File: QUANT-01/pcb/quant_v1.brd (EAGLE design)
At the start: 128.6 x 40.3 mm, 0 parts

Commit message: built the base schematic.
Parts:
- added B1: ARDUINO_PRO_MINI, SparkFun-Boards:ARDUINO_PRO_MINI
- added C1: 0.33uF, SparkFun-Capacitors:CAP-PTH-10MM
- added C2: 0.1uF, SparkFun-Capacitors:CAP-PTH-10MM
- added C3, C4: 100uF, SparkFun-Capacitors:CPOL-RADIAL-5MM-10MM
- added D1, D2: 1n5158, adafruit:DO41-10
- added D10, D3, D4, D5, D6, D7, D8, D9: (no value), SparkFun-LED:LED_3MM
- added MCP4725: (no value), SparkFun-Connectors:1X06_NO_SILK
- added MPR121: (no value), SparkFun-Connectors:1X07
- added MPR121_TOUCH_PINS: (no value), SparkFun-Connectors:1X13
- added R1, R2, R3, R4, R5, R6, R7, R8: 330ohm, SparkFun-Resistors:AXIAL-0.3
- added SW1, SW2, SW3, SW4: SUBMINI_SPDT, MusicThingModular:SUBMINI_TOGGLE
- added TL7805: (no value), SparkFun-IC-Power:DC-DC_CONVERTER_78XX
- added U$1: EURO_POWER_LOCK, MusicThingModular:EURO_PWR_HEADER_LOCK
- added U$3, U$4: FB, adafruit:FB
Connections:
- new net +12V: C1.1, TL7805.VIN
- new net -12V: U$1.NEG1, U$1.NEG2, U$4.P$2
- new net 5V: B1.21, B1.24, C2.1, C3.+, C4.-, D1.C, D2.A, MCP4725.3, MPR121.7, SW1.3, SW2.3, SW3.3, SW4.3, TL7805.VOUT
- new net A0: MCP4725.6
- new net GND: B1.23, B1.4, C1.2, C2.2, C3.-, C4.+, D10.K, D3.K, D4.K, D5.K, D6.K, D7.K, D8.K, D9.K, MCP4725.2, MPR121.5, MPR121_TOUCH_PINS.1, SW1.1, SW2.1, SW3.1, SW4.1, TL7805.GND, U$1.GND1, U$1.GND2, U$1.GND3, U$1.GND4, U$1.GND5, U$1.GND6
- new net N$1: U$1.POS1, U$1.POS2, U$3.P$2
- new net N$10: B1.10, R6.P$2
- new net N$11: B1.11, R7.P$2
- new net N$12: B1.12, R8.P$2
- new net N$13: D10.A, R8.P$1
- new net N$14: D9.A, R7.P$1
- new net N$15: D8.A, R6.P$1
- new net N$16: D7.A, R5.P$1
- new net N$17: D6.A, R4.P$1
- new net N$18: D5.A, R3.P$1
- new net N$19: D4.A, R2.P$1
- new net N$2: D2.C, U$4.P$1
- new net N$3: D1.A, U$3.P$1
- new net N$4: B1.5, R1.P$2
- new net N$5: D3.A, R1.P$1
- new net N$6: B1.6, R2.P$2
- new net N$7: B1.7, R3.P$2
- new net N$8: B1.8, R4.P$2
- new net N$9: B1.9, R5.P$2
- new net SCL: B1.A5, MCP4725.5, MPR121.2
- new net SDA: B1.A4, MCP4725.4, MPR121.3
- new net SW1: B1.13, SW4.COM
- new net SW2: B1.14, SW3.COM
- new net SW3: B1.15, SW2.COM
- new net SW4: B1.16, SW1.COM
- new net TOUCH0: MPR121_TOUCH_PINS.2
- new net TOUCH1: MPR121_TOUCH_PINS.3
- new net TOUCH10: MPR121_TOUCH_PINS.12
- new net TOUCH11: MPR121_TOUCH_PINS.13
- new net TOUCH2: MPR121_TOUCH_PINS.4
- new net TOUCH3: MPR121_TOUCH_PINS.5
- new net TOUCH4: MPR121_TOUCH_PINS.6
- new net TOUCH5: MPR121_TOUCH_PINS.7
- new net TOUCH6: MPR121_TOUCH_PINS.8
- new net TOUCH7: MPR121_TOUCH_PINS.9
- new net TOUCH8: MPR121_TOUCH_PINS.10
- new net TOUCH9: MPR121_TOUCH_PINS.11
- new net VOUT: MCP4725.1

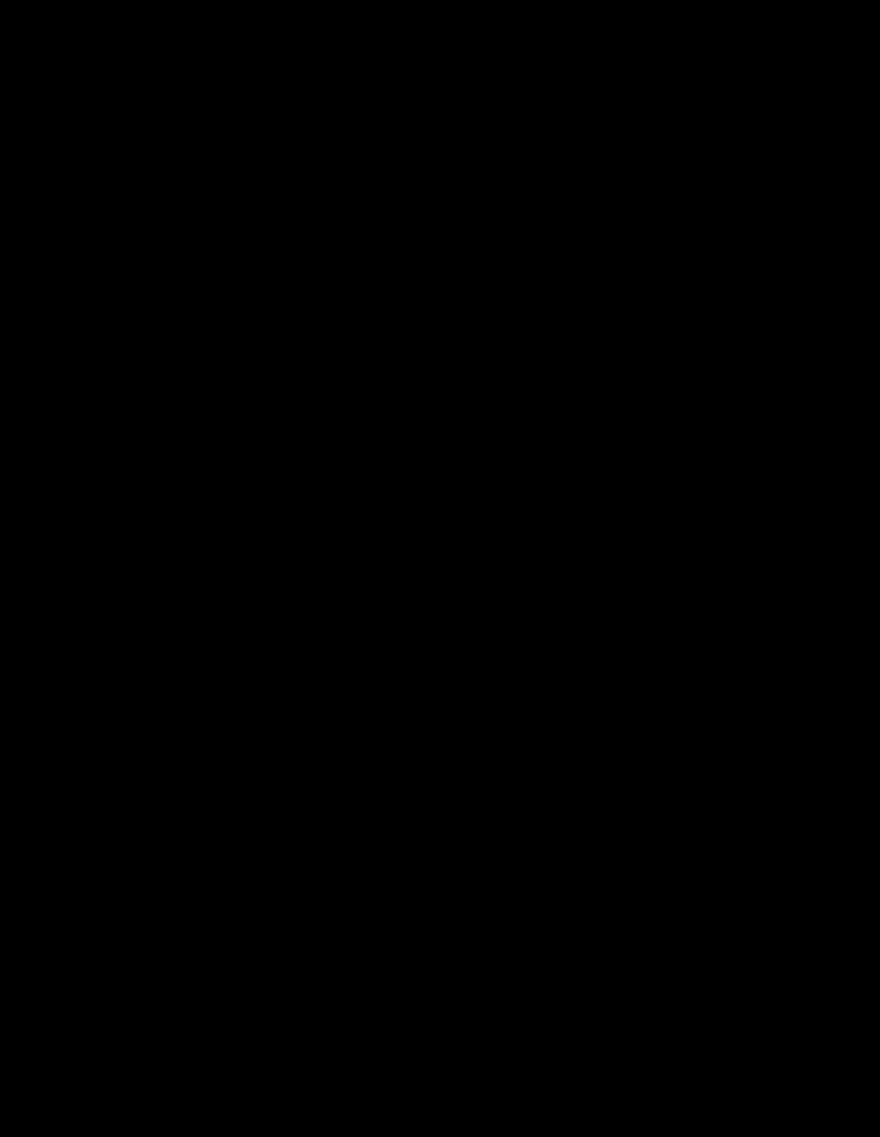
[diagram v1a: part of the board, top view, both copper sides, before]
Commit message: added simple GATE out code.
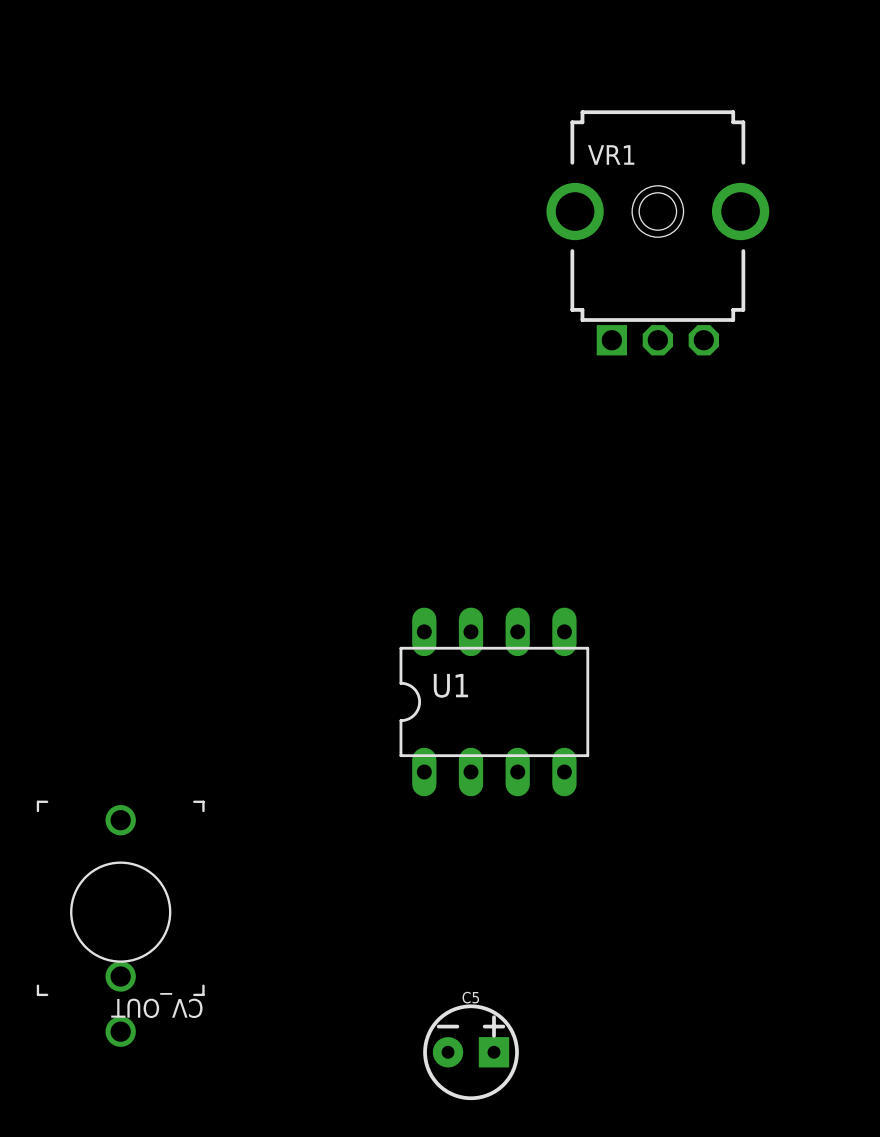
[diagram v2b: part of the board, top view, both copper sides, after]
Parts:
- added C5: 10uF, SparkFun-Capacitors:CPOL-RADIAL-2.5MM-5MM
- added CV_OUT: THONKICONNNEW, MusicThingModular:WQP-PJ301M-12_JACK
- added U1: TL072_, MusicThingModular:DIL08
- added VR1: (no value), MusicThingModular:9MM_SNAP-IN_POT
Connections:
- removed net VOUT: MCP4725.1
- new net N$20: MCP4725.1, U1.3
- new net N$21: U1.1, U1.2, VR1.2, VR1.3
- new net N$23: C5.1, U1.5, VR1.1
- new net N$25: CV_OUT.P$1_TIP, U1.6, U1.7
- new net V+: U1.8
- new net V-: U1.4
- net GND: now also C5.2, CV_OUT.P$3_SLEEVE
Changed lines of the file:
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@@
 <attribute name="PROD_ID" value="RES-08380" x="13.97" y="-604.52" size="1.778" layer="27" display="off"/>
 </element>
+<element name="VR1" library="MusicThingModular" package="9MM_SNAP-IN_POT" value="" x="20.32" y="-629.92"/>
+<element name="U1" library="MusicThingModular" package="DIL08" value="TL072_" x="11.43" y="-656.59"/>
+<element name="C5" library="SparkFun-Capacitors" package="CPOL-RADIAL-2.5MM-5MM" value="10uF" x="10.16" y="-675.64">
+<attribute name="PROD_ID" value="CAP-08440" x="10.16" y="-675.64" size="1.778" layer="27" display="off"/>
+</element>
+<element name="CV_OUT" library="MusicThingModular" package="WQP-PJ301M-12_JACK" value="THONKICONNNEW" x="-8.89" y="-668.02"/>
 </elements>
 <signals>
@@
 <contactref element="D5" pad="K"/>
 <contactref element="D4" pad="K"/>
+<contactref element="C5" pad="2"/>
+<contactref element="CV_OUT" pad="P$3_SLEEVE"/>
 <wire x1="12.7" y1="-452.12" x2="12.7" y2="-471.17" width="0" layer="19" extent="1-1"/>
 <wire x1="12.7" y1="-433.07" x2="12.7" y2="-452.12" width="0" layer="19" extent="1-1"/>
@@
 <wire x1="83.82" y1="27.94" x2="69.85" y2="12.62" width="0" layer="19" extent="1-1"/>
 <wire x1="105.41" y1="15.24" x2="86.36" y2="3.81" width="0" layer="19" extent="1-1"/>
+<wire x1="-8.89" y1="-674.52" x2="12.7" y2="-471.17" width="0" layer="19" extent="1-1"/>
+<wire x1="8.91" y1="-675.64" x2="-8.89" y2="-674.52" width="0" layer="19" extent="1-1"/>
 </signal>
 <signal name="SDA">
@@
 <contactref element="MCP4725" pad="6"/>
 </signal>
-<signal name="VOUT">
-<contactref element="MCP4725" pad="1"/>
-</signal>
 <signal name="TOUCH0">
 <contactref element="MPR121_TOUCH_PINS" pad="2"/>
@@
 <wire x1="10.16" y1="-356.87" x2="10.16" y2="-490.22" width="0" layer="19" extent="1-1"/>
 </signal>
+<signal name="V+">
+<contactref element="U1" pad="8"/>
+</signal>
+<signal name="V-">
+<contactref element="U1" pad="4"/>
+</signal>
+<signal name="N$20">
+<contactref element="MCP4725" pad="1"/>
+<contactref element="U1" pad="3"/>
+<wire x1="81.28" y1="27.94" x2="12.7" y2="-660.4" width="0" layer="19" extent="1-1"/>
+</signal>
+<signal name="N$21">
+<contactref element="U1" pad="1"/>
+<contactref element="VR1" pad="3"/>
+<contactref element="VR1" pad="2"/>
+<contactref element="U1" pad="2"/>
+<wire x1="10.16" y1="-660.4" x2="7.62" y2="-660.4" width="0" layer="19" extent="1-1"/>
+<wire x1="20.32" y1="-636.92" x2="10.16" y2="-660.4" width="0" layer="19" extent="1-1"/>
+<wire x1="22.82" y1="-636.92" x2="20.32" y2="-636.92" width="0" layer="19" extent="1-1"/>
+</signal>
+<signal name="N$23">
+<contactref element="VR1" pad="1"/>
+<contactref element="U1" pad="5"/>
+<contactref element="C5" pad="1"/>
+<wire x1="15.24" y1="-652.78" x2="11.41" y2="-675.64" width="0" layer="19" extent="1-1"/>
+<wire x1="17.82" y1="-636.92" x2="15.24" y2="-652.78" width="0" layer="19" extent="1-1"/>
+</signal>
+<signal name="N$25">
+<contactref element="U1" pad="7"/>
+<contactref element="CV_OUT" pad="P$1_TIP"/>
+<contactref element="U1" pad="6"/>
+<wire x1="10.16" y1="-652.78" x2="-8.89" y2="-663.02" width="0" layer="19" extent="1-1"/>
+<wire x1="12.7" y1="-652.78" x2="10.16" y2="-652.78" width="0" layer="19" extent="1-1"/>
+</signal>
 </signals>

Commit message: started building board.
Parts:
- removed U1: TL072_, MusicThingModular:DIL08
- added C7: 47pf, SparkFun-Capacitors:CAP-PTH-10MM
- added C8, C9: 100nf, SparkFun-Capacitors:CAP-PTH-10MM
- added CV_INPUT: THONKICONNNEW, MusicThingModular:WQP-PJ301M-12_JACK
- added D11: (no value), SparkFun-LED:LED_3MM
- added GATE_OUT: GATE_OUT, MusicThingModular:WQP-PJ301M-12_JACK
- added R10, R11, R17, R18, R9: 100k, SparkFun-Resistors:AXIAL-0.3
- added R12: 49.9k, SparkFun-Resistors:AXIAL-0.3
- added R13, R19, R20: 10k, SparkFun-Resistors:AXIAL-0.3
- added R14, R21: 1k, SparkFun-Resistors:AXIAL-0.3
- added SW5_MODE: SUBMINI_SPDT, MusicThingModular:SUBMINI_TOGGLE
- added U3: MCP6002, MusicThingModular:DIL08
- added U4: TL074_, MusicThingModular:DIL14
- moved C5 738.4 mm to (-16.5, 62.2)
- moved R8 682.0 mm to (-58.4, 73.7)
- moved CV_OUT 676.8 mm to (-48.3, 7.62)
- moved R7 662.1 mm to (-48.3, 73.7)
- moved VR1 645.1 mm to (-69.8, 8.89)
- moved R6 642.2 mm to (-38.1, 73.7)
- moved R5 622.4 mm to (-27.9, 73.7)
- moved R4 602.8 mm to (-17.8, 73.7)
- moved R3 583.7 mm to (-68.6, 68.6)
- moved R2 563.5 mm to (-58.4, 68.6)
- moved D10 541.8 mm to (-35.6, 68.6)
- moved D9 522.4 mm to (-30.5, 68.6)
- moved D8 503.0 mm to (-25.4, 68.6)
- moved D7 483.6 mm to (-20.3, 68.6)
- moved D6 464.3 mm to (-15.2, 68.6)
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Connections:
- removed net V+: U1.8
- removed net V-: U1.4
- new net N$22: CV_INPUT.P$1_TIP, R9.P$1
- new net N$24: R10.P$2, R9.P$2, U4.2
- new net N$26: B1.18, R13.P$2
- new net N$27: R13.P$1, SW5_MODE.COM
- new net N$28: R10.P$1, R11.P$2, U4.1
- new net N$29: R11.P$1, R12.P$2, U3.2
- new net N$30: R17.P$1, R18.P$1, U3.5
- new net N$31: GATE_OUT.P$1_TIP, R21.P$1
- new net N$32: R14.P$2, U4.13
- new net N$33: D11.A, R14.P$1, U4.14
- new net N$37: B1.19, R20.P$2, U4.12
- new net N$38: C7.2, R19.P$2, R20.P$1, U3.6
- new net N$39: C7.1, R19.P$1, R21.P$2, U3.7
- new net VEE: B1.17, R12.P$1, U3.1
- net 5V: now also C8.1, C9.1, R17.P$2, U3.8, U4.11, U4.4
- net GND: now also C8.2, C9.2, CV_INPUT.P$3_SLEEVE, D11.K, GATE_OUT.P$3_SLEEVE, R18.P$2, SW5_MODE.1, U3.3, U3.4, U4.3
- net N$20: now also U4.5; no longer U1.3
- net N$21: now also U4.6, U4.7; no longer U1.1, U1.2
- net N$23: now also U4.10; no longer U1.5
- net N$25: now also U4.8, U4.9; no longer U1.6, U1.7
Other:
- board size 128.6 x 40.3 mm -> 127 x 81.3 mm
- board text removed: "10HP"
- board text removed: "EURORACK PCB BREADBOARD V1.0"

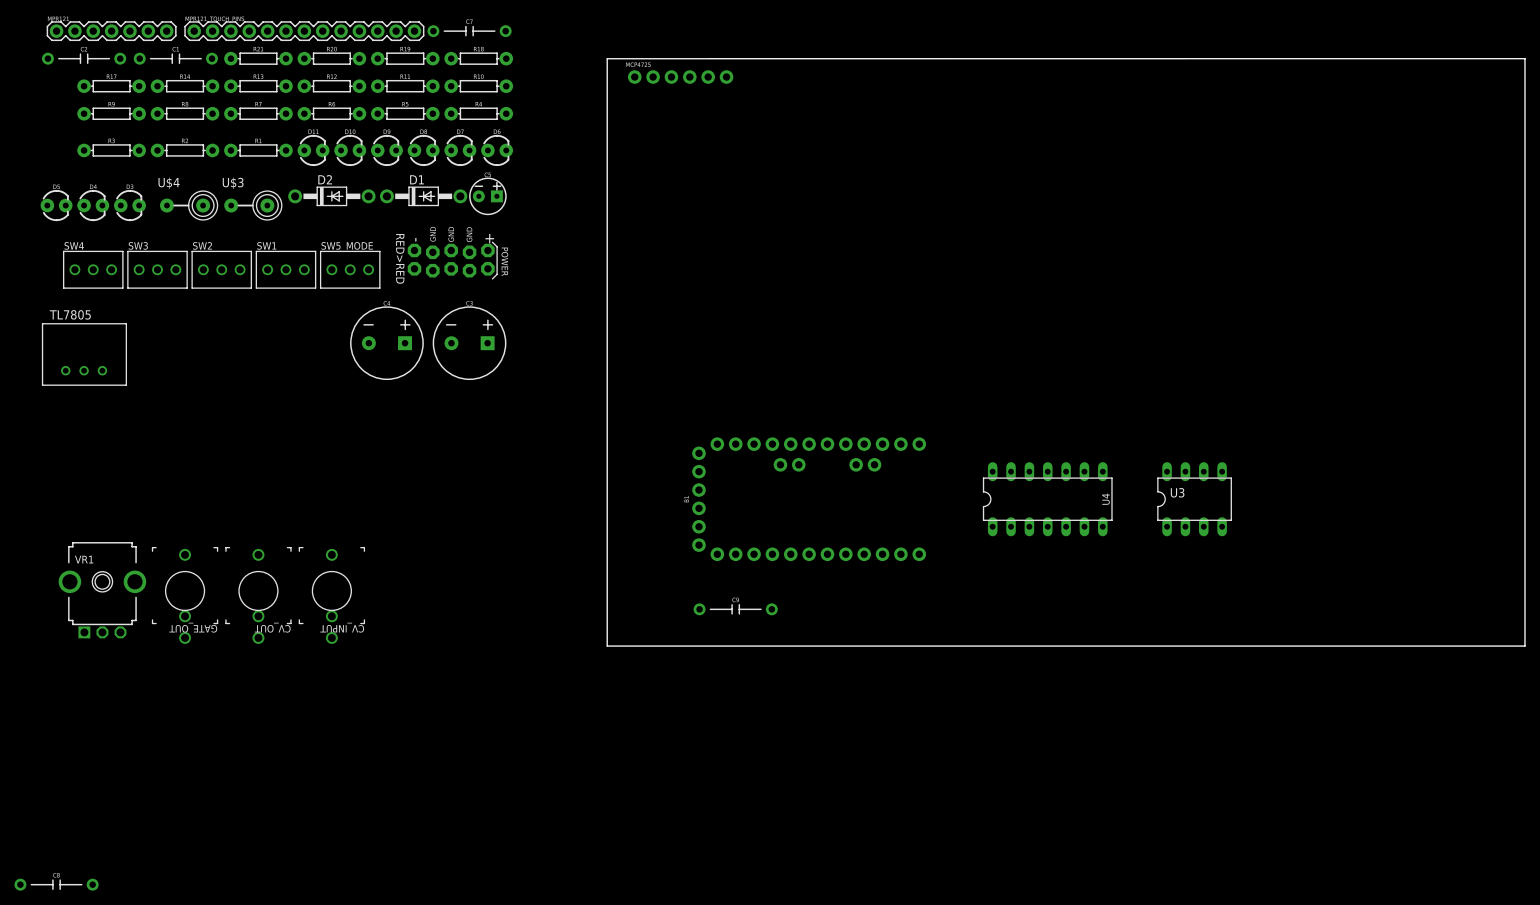
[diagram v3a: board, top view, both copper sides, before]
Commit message: got bottom pcb basic layout in place.
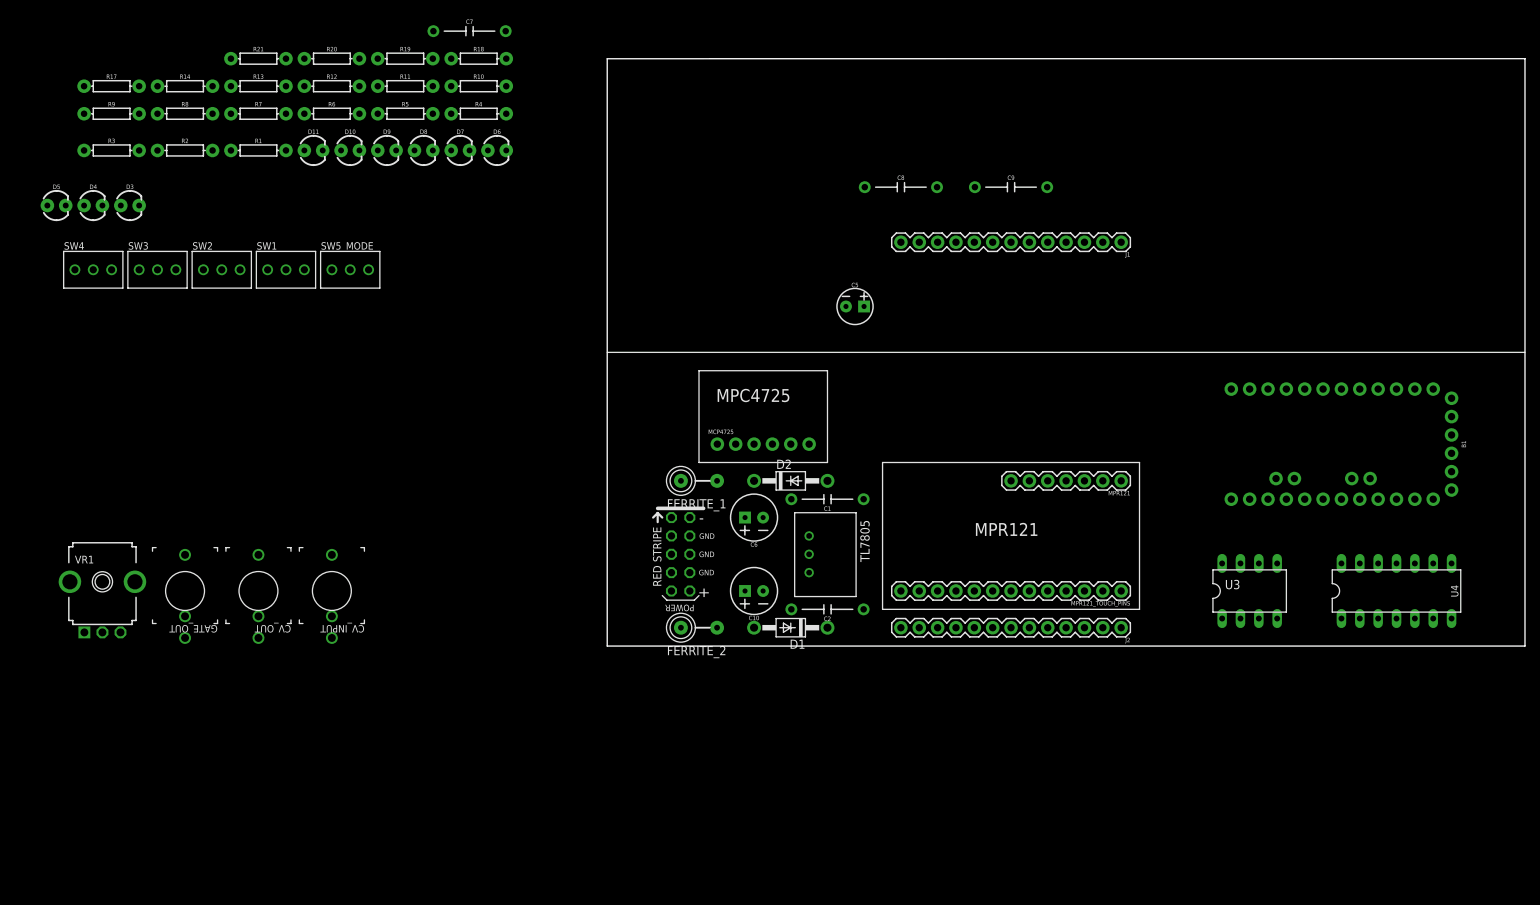
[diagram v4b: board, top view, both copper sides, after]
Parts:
- removed C3, C4: 100uF, SparkFun-Capacitors:CPOL-RADIAL-5MM-10MM
- removed U$1: EURO_POWER_LOCK, MusicThingModular:EURO_PWR_HEADER_LOCK
- removed U$3, U$4: FB, adafruit:FB
- added C10, C6: 100uF, SparkFun-Capacitors:CPOL-RADIAL-2.5MM-6.5MM
- added FERRITE_1, FERRITE_2: FB, adafruit:FB
- added J1, J2: (no value), SparkFun-Connectors:1X13
- added POWER: (no value), MusicThingModular:EURO_POWER_HEADER
- moved MPR121 159.9 mm to (71.1, 22.9), turned to 180 degrees
- moved C8 151.6 mm to (40.6, 63.5)
- moved MPR121_TOUCH_PINS 149.8 mm to (71.1, 7.62), turned to 180 degrees
- moved C2 128.0 mm to (30.5, 5.08), turned to 180 degrees
- moved C1 108.8 mm to (30.5, 20.3), turned to 180 degrees
- moved TL7805 103.5 mm to (27.9, 12.7), turned to 270 degrees
- moved D1 78.4 mm to (25.4, 2.54), turned to 180 degrees
- moved D2 74.7 mm to (25.4, 22.9)
- moved B1 74.1 mm to (101.6, 27.9), turned to 270 degrees
- moved C9 69.7 mm to (55.9, 63.5)
- moved C5 53.0 mm to (34.3, 47.0)
- moved MCP4725 52.1 mm to (15.2, 27.9)
- moved U4 49.9 mm to (109.2, 7.62)
- moved U3 14.8 mm to (88.9, 7.62)
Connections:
- removed net -12V: U$1.NEG1, U$1.NEG2, U$4.P$2
- new net N$34: FERRITE_1.P$2, POWER.1, POWER.2
- net 5V: now also C10.2, C6.1; no longer C3.+, C4.-
- net GND: now also C10.1, C6.2, POWER.3, POWER.4, POWER.5, POWER.6, POWER.7, POWER.8; no longer C3.-, C4.+, U$1.GND1, U$1.GND2, U$1.GND3, U$1.GND4, U$1.GND5, U$1.GND6
- net N$1: now also FERRITE_2.P$2, POWER.10, POWER.9; no longer U$1.POS1, U$1.POS2, U$3.P$2
- net N$2: now also FERRITE_1.P$1; no longer U$4.P$1
- net N$3: now also FERRITE_2.P$1; no longer U$3.P$1
- net TOUCH0: now also J1.2, J2.2
- net TOUCH1: now also J1.3, J2.3
- net TOUCH10: now also J1.12, J2.12
- net TOUCH11: now also J1.13, J2.13
- net TOUCH2: now also J1.4, J2.4
- net TOUCH3: now also J1.5, J2.5
- net TOUCH4: now also J1.6, J2.6
- net TOUCH5: now also J1.7, J2.7
- net TOUCH6: now also J1.8, J2.8
- net TOUCH7: now also J1.9, J2.9
- net TOUCH8: now also J1.10, J2.10
- net TOUCH9: now also J1.11, J2.11
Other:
- board text added: "MPC4725"
- board text added: "MPR121"
